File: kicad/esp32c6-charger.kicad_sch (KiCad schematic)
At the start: 0 parts

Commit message: moved some of the configuration to it's own file
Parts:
- added Brd1: SSD1306, Custom:128x64OLED, symbol CustomSymbols:SSD1306
- added D1: WS2812B, LED_SMD:LED_WS2812B_PLCC4_5.0x5.0mm_P3.2mm, symbol LED:WS2812B
- added D2: Lock, LED_SMD:LED_1206_3216Metric_Pad1.42x1.75mm_HandSolder, symbol Device:LED
- added D3: Relay, LED_SMD:LED_1206_3216Metric_Pad1.42x1.75mm_HandSolder, symbol Device:LED
- added D4: Detect, LED_SMD:LED_1206_3216Metric_Pad1.42x1.75mm_HandSolder, symbol Device:LED
- added J1: Conn_01x06_Socket, TerminalBlock_Phoenix:TerminalBlock_Phoenix_MKDS-1,5-6-5.08_1x06_P5.08mm_Horizontal, symbol Connector:Conn_01x06_Socket
- added J2: Conn_01x03_Socket, TerminalBlock_Phoenix:TerminalBlock_Phoenix_MKDS-1,5-3-5.08_1x03_P5.08mm_Horizontal, symbol Connector:Conn_01x03_Socket
- added K1: G2RL-1, Relay_THT:Relay_SPDT_Omron_G2RL-1, symbol Relay:G2RL-1
- added Q1, Q2: BC817, Package_TO_SOT_SMD:SOT-23-3, symbol Transistor_BJT:BC547
- added R1, R2: 10k, Resistor_SMD:R_1206_3216Metric_Pad1.30x1.75mm_HandSolder, symbol Device:R
- added R3, R4, R5: 68, Resistor_SMD:R_1206_3216Metric_Pad1.30x1.75mm_HandSolder, symbol Device:R
- added RFID1: RC522, Custom:RC522, symbol CustomSymbols:RC522
- added U1: XIAO-ESP32-C6, Seeed Studio XIAO Series Library:XIAO-ESP32C6-DIP, symbol Seeed_Studio_XIAO_Series:XIAO_ESP32-C6-DIP
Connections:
- new net: D2.1 (K), J1.3 (Pin_3), Q1.1 (C)
- new net: D4.1 (K), J1.4 (Pin_4), U1.2 (GPIO1/A1/D1)
- new net: R2.1, U1.3 (GPIO2/A2/D2)
- new net: Q2.2 (B), R2.2
- new net: D4.2 (A), R5.1
- new net: D1.4 (DIN), U1.1 (GPIO0/A0/D0)
- new net: D3.1 (K), K1.A2, Q2.1 (C)
- new net: D2.2 (A), R4.1
- new net: R1.1, U1.4 (GPIO21/D3)
- new net: Q1.2 (B), R1.2
- new net: J2.1 (Pin_1), K1.11
- new net: J2.2 (Pin_2), K1.14
- new net: J2.3 (Pin_3), K1.12
- new net: D3.2 (A), R3.1
- new net +5V: D1.1 (VDD), J1.1 (Pin_1), K1.A1, U1.14 (VBUS)
- new net CS: RFID1.1 (SDA), U1.8 (GPIO17/D7/RX)
- new net GND: Brd1.1 (GND), D1.3 (VSS), J1.5 (Pin_5), J1.6 (Pin_6), Q1.3 (E), Q2.3 (E), RFID1.6 (GND), U1.13 (GND)
- new net MISO: RFID1.4 (MISO), U1.10 (GPIO20/D9/MISO)
- new net MOSI: RFID1.3 (MOSI), U1.11 (GPIO18/D10/MOSI)
- new net SCK: RFID1.2 (SCK), U1.9 (GPIO19/D8/SCK)
- new net SCL: Brd1.3 (SCL), U1.6 (GPIO23/D5/SCL)
- new net SDA: Brd1.4 (SDA), U1.5 (GPIO22/D4/SDA)
- new net VCC: Brd1.2 (VCC), J1.2 (Pin_2), R3.2, R4.2, R5.2, RFID1.8 (3,3V), U1.12 (3V3)

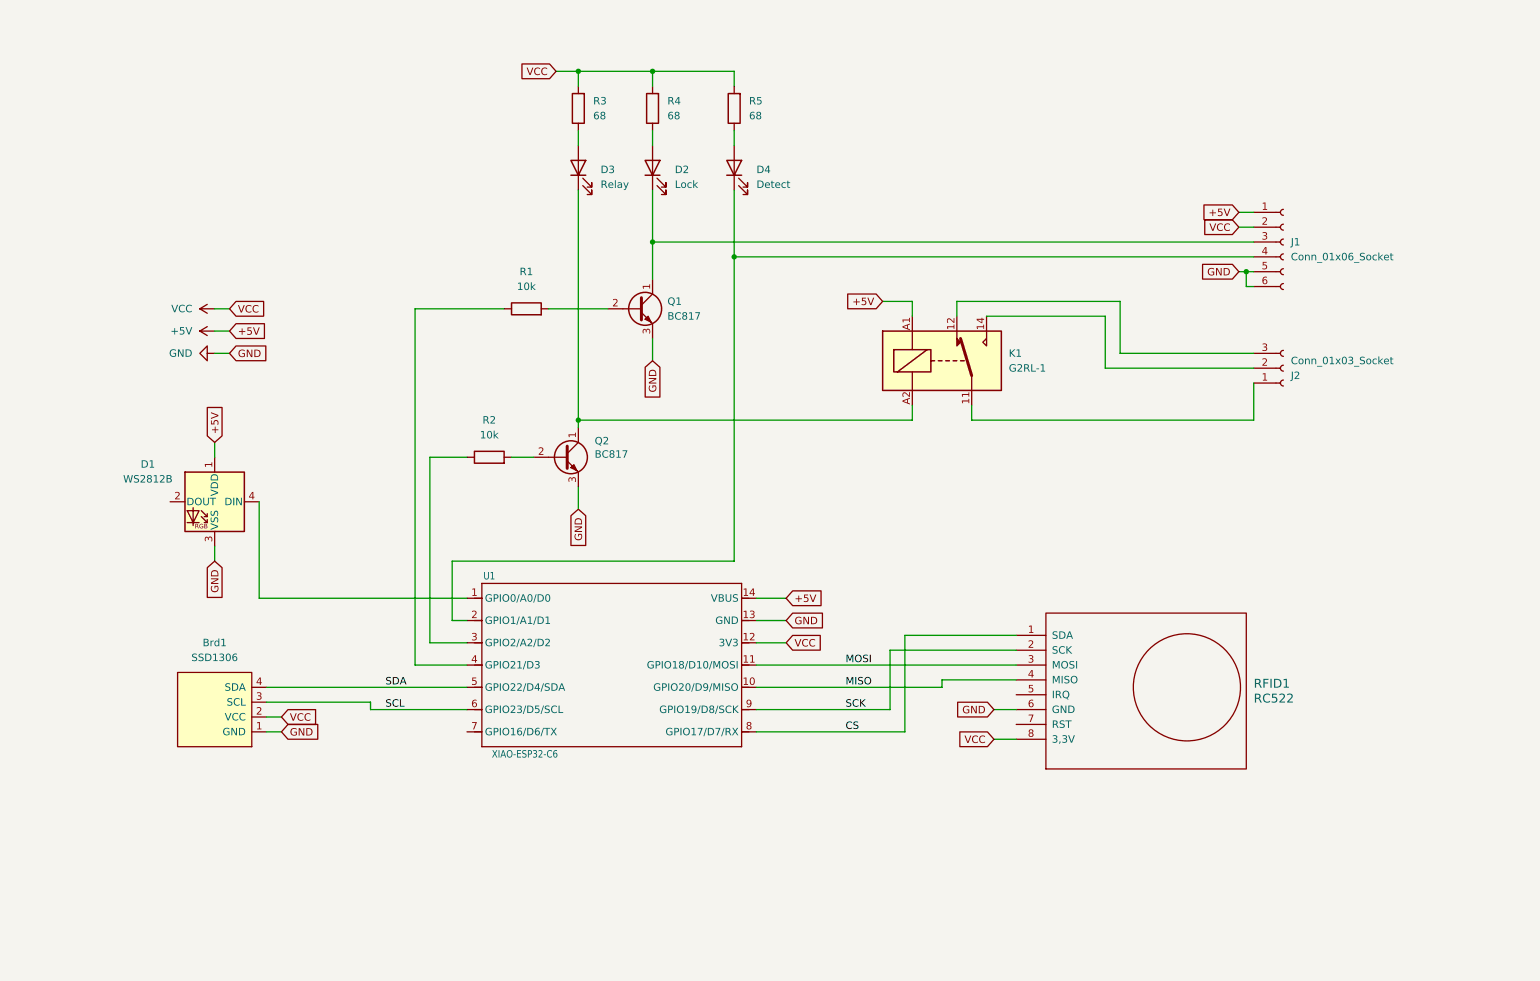
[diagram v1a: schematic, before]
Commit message: added external power possibility
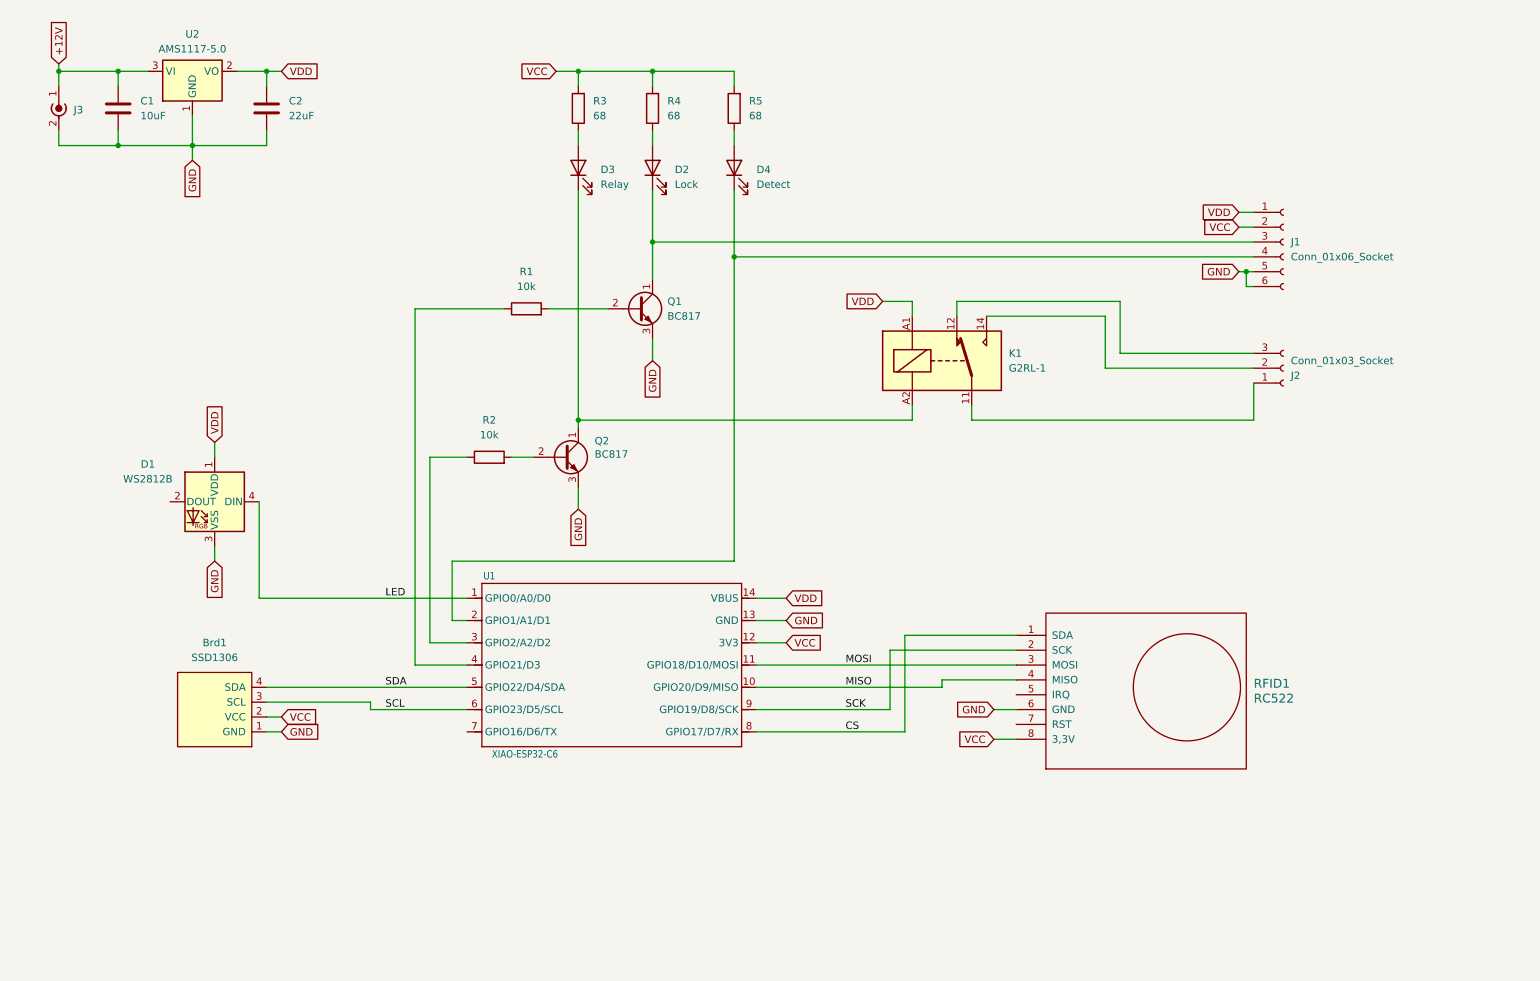
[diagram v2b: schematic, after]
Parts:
- added C1: 10uF, Capacitor_SMD:C_0805_2012Metric_Pad1.18x1.45mm_HandSolder, symbol Device:C
- added C2: 22uF, Capacitor_SMD:C_0805_2012Metric_Pad1.18x1.45mm_HandSolder, symbol Device:C
- added J3: Conn_Coaxial_Power, Connector_BarrelJack:BarrelJack_Horizontal, symbol Connector:Conn_Coaxial_Power
- added U2: AMS1117-5.0, Package_TO_SOT_SMD:SOT-223-3_TabPin2, symbol Regulator_Linear:AMS1117-5.0
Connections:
- net GND: now also C1.2, C2.2, J3.2 (Ext), U2.1 (GND)
- net LED: now reaches D1.4 (DIN), U1.1 (GPIO0/A0/D0)
- net +5V renamed VDD
- net VDD: now also C2.1, U2.2 (VO)
- new net +12V: C1.1, J3.1 (In), U2.3 (VI)

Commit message: updated changes to schematic and pcb
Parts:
- added J4: Conn_01x06_Pin, symbol Connector:Conn_01x06_Pin
- added J5: Conn_01x03_Pin, symbol Connector:Conn_01x03_Pin
- added K2: Relay_SPTT, symbol CustomSymbols:Relay_SPTT
- added SW1: Cable Detect, symbol Switch:SW_Push
- added U3: Solenoid, symbol CustomSymbols:Solenoid
- C1, C2: footprint Capacitor_SMD:C_0805_2012Metric_Pad1.18x1.45mm_HandSolder -> Capacitor_Tantalum_SMD:CP_EIA-6032-28_Kemet-C
- J1: value Conn_01x06_Socket -> Power/Lock/Detect
- J2: value Conn_01x03_Socket -> Relay
- R3, R4, R5: value 68 -> 68Ω
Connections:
- net Lock: now reaches D2.1 (K), J1.3 (Pin_3), Q1.1 (C)
- net Detect: now reaches D4.1 (K), J1.4 (Pin_4), U1.2 (GPIO1/A1/D1)
- net VDD renamed +5V
- new net: J4.1 (Pin_1), U3. (A2)
- new net: J4.3 (Pin_3), U3. (A2)
- new net: J5.3 (Pin_3), K2.11
- new net: J5.2 (Pin_2), K2.A1
- new net: J4.6 (Pin_6), SW1.1
- new net: J4.4 (Pin_4), SW1.2
- new net GNDPWR: J4.5 (Pin_5)
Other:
- note added: "1"
- note added: "2"
- note added: "3"
- note added: "Charger Connector and 3-phase relay"
- note added: "G"
- note added: "N"
- company: (none) -> https://gertjanassies.dev/blog?category=make
- title: (none) -> ESP32-C6 EV Charger
- moved on the sheet: Brd1, C1, C2, D1, D2, D3, D4, J1, J2, J3, K1, Q1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

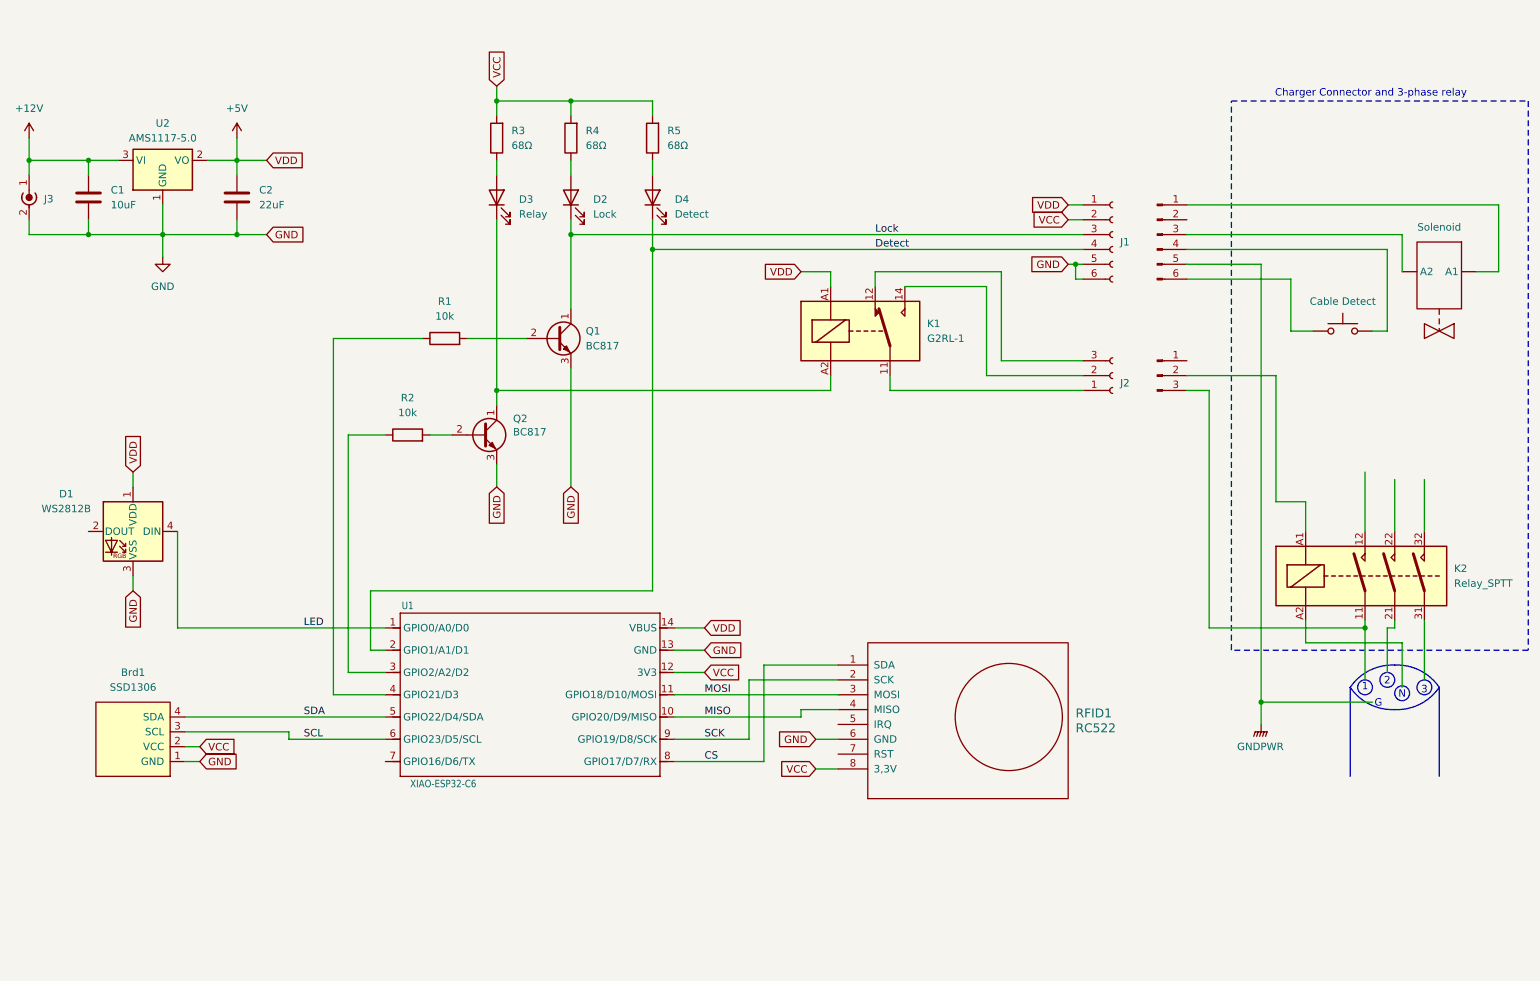
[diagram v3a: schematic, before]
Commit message: small changes and a pdf of the schematic in the export jobset
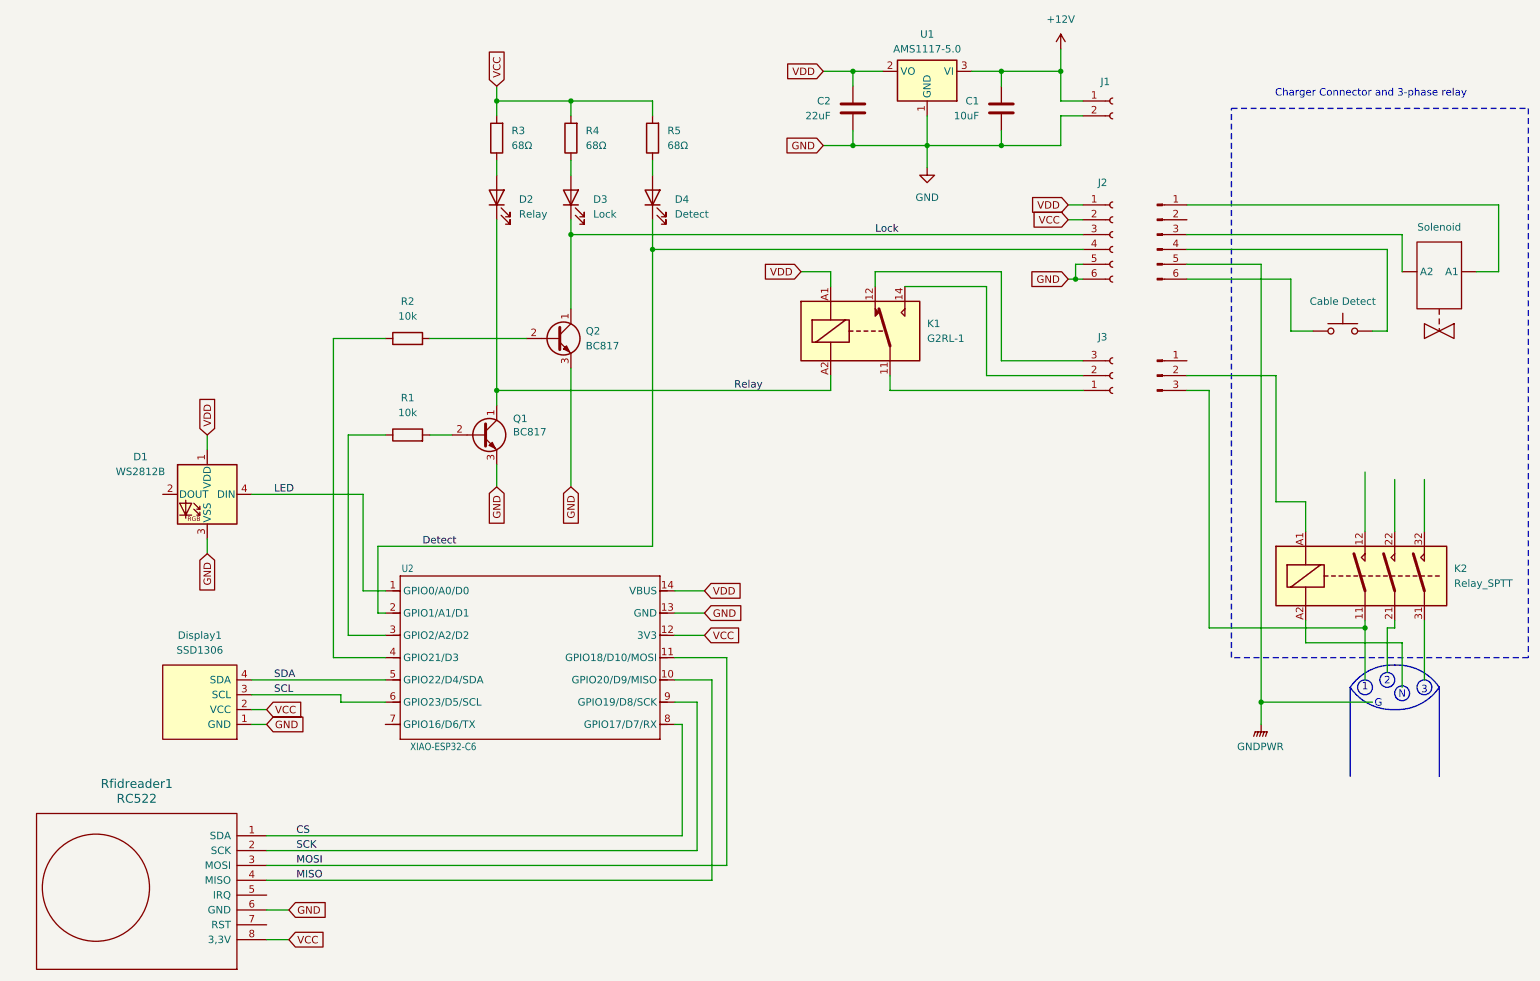
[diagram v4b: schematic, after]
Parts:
- removed J3: Conn_Coaxial_Power, Connector_BarrelJack:BarrelJack_Horizontal, symbol Connector:Conn_Coaxial_Power
- added J1: Conn_01x02_Socket, TerminalBlock_Phoenix:TerminalBlock_Phoenix_MKDS-1,5-2-5.08_1x02_P5.08mm_Horizontal, symbol Connector:Conn_01x02_Socket
- renumbered D3 to D2, D2 to D3, Brd1 to Display1, J1 to J2, J2 to J3, Q2 to Q1, Q1 to Q2, R2 to R1, R1 to R2, RFID1 to Rfidreader1, U2 to U1, U1 to U2
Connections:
- net +12V: now also J1.1 (Pin_1)
- net GND: now also J1.2 (Pin_2)
- net Relay: now reaches D2.1 (K), K1.A2, Q1.1 (C)
- net +5V renamed VDD
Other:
- moved on the sheet: C1, C2, D1, Display1, R2, Rfidreader1, U1, U2

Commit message: updated 3d model for relay
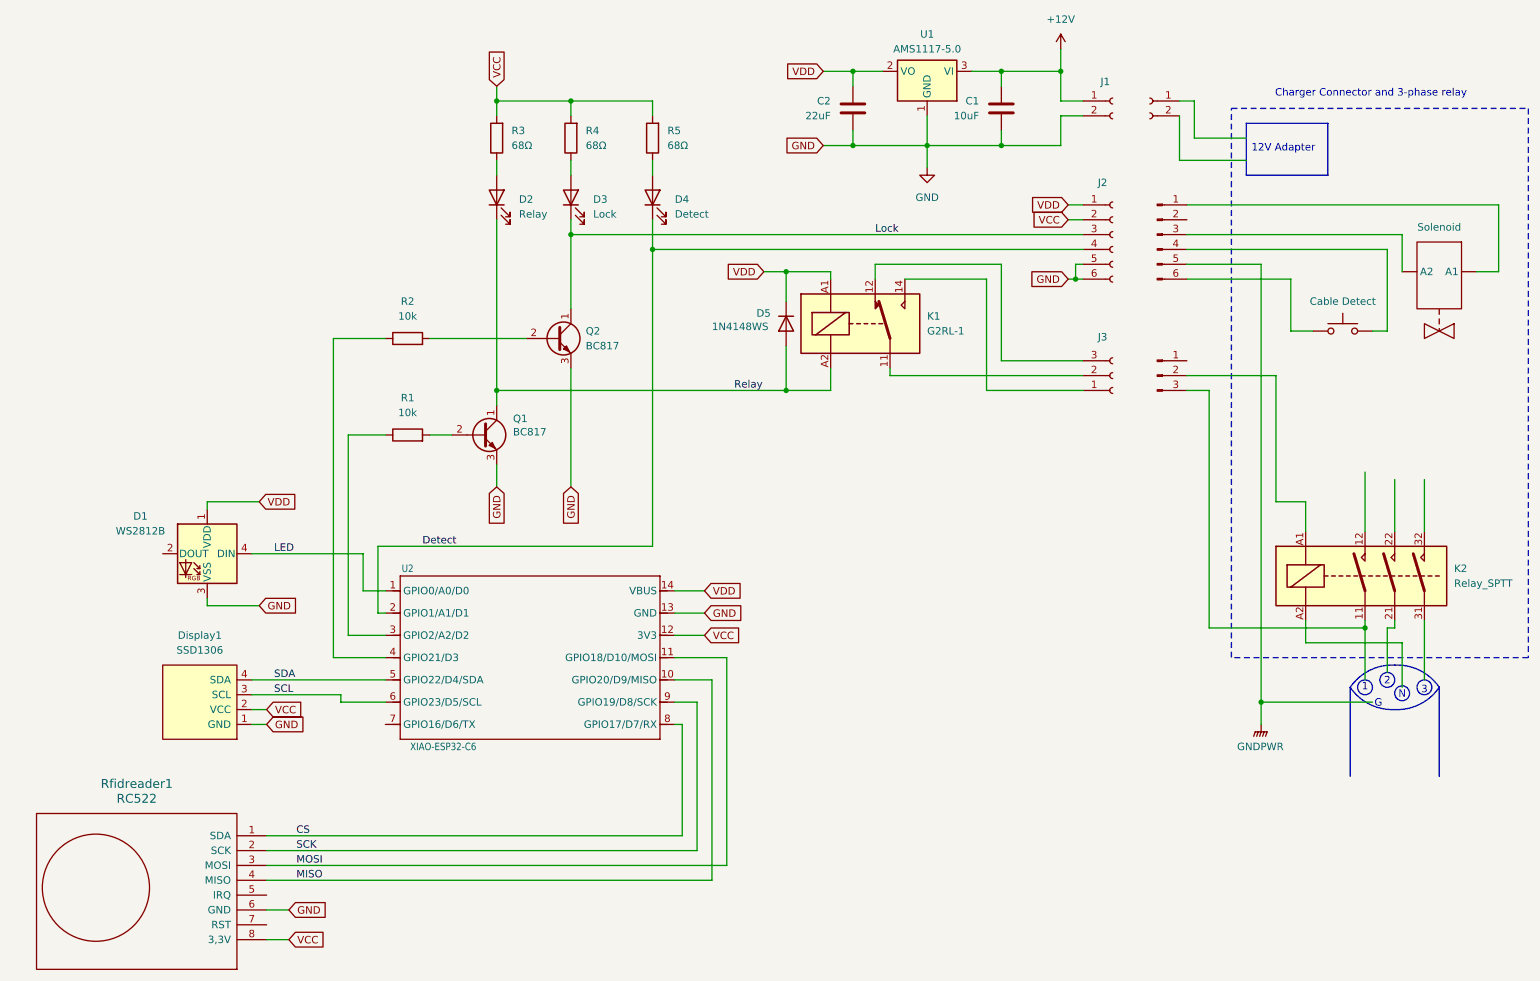
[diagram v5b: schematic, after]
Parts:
- added D5: 1N4148WS, Diode_SMD:D_SOD-323, symbol Diode:1N4148WS
- added J6: Conn_01x02_Socket, TerminalBlock_Phoenix:TerminalBlock_Phoenix_MKDS-1,5-2-5.08_1x02_P5.08mm_Horizontal, symbol Connector:Conn_01x02_Socket
- K1: footprint Relay_THT:Relay_SPDT_Omron_G2RL-1 -> Relay_THT:Relay_SPDT_Omron_G2RL-1-E
- Q1, Q2: footprint Package_TO_SOT_SMD:SOT-23-3 -> Package_TO_SOT_SMD:SOT-23
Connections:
- net Relay: now also D5.2 (A)
- net VDD: now also D5.1 (K)
- net at J3.1 (Pin_1): now also K1.14; no longer K1.11
- net at J3.2 (Pin_2): now also K1.11; no longer K1.14
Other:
- note added: "12V Adapter"
- moved on the sheet: D1, K1

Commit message: used normal transistors and diodes instead of SMD ones, we have the space, why make soldering life more difficult
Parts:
- D5: footprint Diode_SMD:D_SOD-323 -> Diode_THT:D_DO-35_SOD27_P7.62mm_Horizontal
- Q1, Q2: value BC817 -> BC337; footprint Package_TO_SOT_SMD:SOT-23 -> Package_TO_SOT_THT:TO-92
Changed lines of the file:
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@@
 			)
 		)
-		(property "Value" "BC817"
+		(property "Value" "BC337"
 			(at 106.934 90.932 0)
 			(effects
@@
 			)
 		)
-		(property "Footprint" "Package_TO_SOT_SMD:SOT-23"
+		(property "Footprint" "Package_TO_SOT_THT:TO-92"
 			(at 106.68 93.345 0)
 			(effects
@@
 			)
 		)
-		(property "Footprint" "Diode_SMD:D_SOD-323"
+		(property "Footprint" "Diode_THT:D_DO-35_SOD27_P7.62mm_Horizontal"
 			(at 158.115 72.39 0)
 			(effects
@@
 			)
 		)
-		(property "Value" "BC817"
+		(property "Value" "BC337"
 			(at 119.38 76.1999 0)
 			(effects
@@
 			)
 		)
-		(property "Footprint" "Package_TO_SOT_SMD:SOT-23"
+		(property "Footprint" "Package_TO_SOT_THT:TO-92"
 			(at 119.38 76.835 0)
 			(effects
